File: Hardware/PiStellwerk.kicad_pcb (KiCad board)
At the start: 2 copper layers, 65 x 56 mm, 59 parts, among them J1 Conn_02x20_Odd_Even, J2 Screw_Terminal_01x02, J3 Screw_Terminal_01x02, J4 Conn_01x01, J5 Conn_01x01, J6 Conn_02x03_Odd_Even, J7 Screw_Terminal_01x02, Q1 Q_PMOS_GDS, U1 STM32G031KxT, U2 HT7533, U3 DRV8876, U4 RT8279, U5 6N136, U6 6N136, U7 RT8279, U8 DS18B20

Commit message: Change from STM32G0 to STM32F103C8T6
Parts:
- removed D2, D3: SS54, Diode_SMD:D_SMB_Handsoldering
- removed L2: 10uH, Inductor_SMD:L_7.3x7.3_H4.5
- removed R10: 100K, Resistor_SMD:R_0603_1608Metric_Pad1.05x0.95mm_HandSolder
- removed R12: R, Resistor_SMD:R_0603_1608Metric_Pad1.05x0.95mm_HandSolder
- removed R6: 10K, Resistor_SMD:R_0603_1608Metric_Pad1.05x0.95mm_HandSolder
- added C15: 35V/10nF, Capacitor_SMD:C_0603_1608Metric_Pad1.05x0.95mm_HandSolder, F.Cu at (38.7, 73.6)
- added C16: 35V/10nF, Capacitor_SMD:C_0603_1608Metric_Pad1.05x0.95mm_HandSolder, F.Cu at (48.5, 75.0)
- added C21: 6.3V/47uF, Capacitor_SMD:C_0805_2012Metric_Pad1.15x1.40mm_HandSolder, F.Cu at (20.6, 86.5)
- added C24: 35V/10uF, Capacitor_SMD:C_0805_2012Metric_Pad1.15x1.40mm_HandSolder, F.Cu at (25.2, 82.9)
- added C25: 35V/10nF, Capacitor_SMD:C_0603_1608Metric_Pad1.05x0.95mm_HandSolder, F.Cu at (50.7, 62.0)
- added C26: 6.3V/47uF, Capacitor_SMD:C_0805_2012Metric_Pad1.15x1.40mm_HandSolder, F.Cu at (30.9, 81.4)
- added C27: 35V/100nF, Capacitor_SMD:C_0603_1608Metric_Pad1.05x0.95mm_HandSolder, F.Cu at (44.2, 80.7)
- added C28: 35V/100nF, Capacitor_SMD:C_0603_1608Metric_Pad1.05x0.95mm_HandSolder, F.Cu at (25.1, 85.6)
- added C29: 35V/100nF, Capacitor_SMD:C_0603_1608Metric_Pad1.05x0.95mm_HandSolder, F.Cu at (35.5, 76.1)
- added C30: 35V/100nF, Capacitor_SMD:C_0603_1608Metric_Pad1.05x0.95mm_HandSolder, F.Cu at (25.1, 88.1)
- added C31: 35V/100nF, Capacitor_SMD:C_0603_1608Metric_Pad1.05x0.95mm_HandSolder, F.Cu at (43.4, 70.7)
- added C32: 35V/100nF, Capacitor_SMD:C_0603_1608Metric_Pad1.05x0.95mm_HandSolder, F.Cu at (35.5, 78.6)
- added C33: 35V/100nF, Capacitor_SMD:C_0603_1608Metric_Pad1.05x0.95mm_HandSolder, F.Cu at (46.7, 67.4)
- added C34: 35V/10nF, Capacitor_SMD:C_0603_1608Metric_Pad1.05x0.95mm_HandSolder, F.Cu at (29.8, 84.1)
- added C35: 35V/100nF, Capacitor_SMD:C_0603_1608Metric_Pad1.05x0.95mm_HandSolder, F.Cu at (55.4, 59.0)
- added C40: 35V/100uF, Capacitor_THT:CP_Radial_D6.3mm_P2.50mm, F.Cu at (26.0, 73.0)
- added C41: 35V/100uF, Capacitor_THT:CP_Radial_D6.3mm_P2.50mm, F.Cu at (13.1, 85.4)
- added J8: Conn_01x06, Connector_PinSocket_2.54mm:PinSocket_1x06_P2.54mm_Vertical, F.Cu at (56.4, 75.8)
- added J9: Conn_01x05, Connector_PinHeader_2.54mm:PinHeader_1x05_P2.54mm_Vertical, F.Cu at (61.0, 75.8)
- added JP1: Jumper, Connector_PinHeader_2.54mm:PinHeader_1x02_P2.54mm_Vertical, F.Cu at (20.5, 80.2)
- added JP2: Jumper, Connector_PinHeader_2.54mm:PinHeader_1x02_P2.54mm_Vertical, F.Cu at (41.4, 60.1)
- added L10: 3.3uH, Inductor_SMD:L_6.3x6.3_H3, F.Cu at (34.8, 61.7)
- added L11: 3.3uH, Inductor_SMD:L_6.3x6.3_H3, F.Cu at (5.97, 85.4)
- added L12: 3.3uH, Inductor_SMD:L_6.3x6.3_H3, F.Cu at (18.9, 73.9)
- added R14: 100K, Resistor_SMD:R_0603_1608Metric_Pad1.05x0.95mm_HandSolder, F.Cu at (44.2, 78.2)
- added R15: 13.7K, Resistor_SMD:R_0603_1608Metric_Pad1.05x0.95mm_HandSolder, F.Cu at (55.4, 67.0)
- added R16: 100K, Resistor_SMD:R_0603_1608Metric_Pad1.05x0.95mm_HandSolder, F.Cu at (34.1, 84.1)
- added R17: 13.7K, Resistor_SMD:R_0603_1608Metric_Pad1.05x0.95mm_HandSolder, F.Cu at (52.1, 72.0)
- added R19: 100K, Resistor_SMD:R_0603_1608Metric_Pad1.05x0.95mm_HandSolder, F.Cu at (47.8, 69.9)
- added R30: 22.1K, Resistor_SMD:R_0603_1608Metric_Pad1.05x0.95mm_HandSolder, F.Cu at (51.0, 67.0)
- added R40: 24R, Resistor_SMD:R_0603_1608Metric_Pad1.05x0.95mm_HandSolder, F.Cu at (39.8, 78.6)
- added R41: 24R, Resistor_SMD:R_0603_1608Metric_Pad1.05x0.95mm_HandSolder, F.Cu at (51.0, 64.5)
- added R42: 24R, Resistor_SMD:R_0603_1608Metric_Pad1.05x0.95mm_HandSolder, F.Cu at (39.8, 81.1)
- added R43: 24R, Resistor_SMD:R_0603_1608Metric_Pad1.05x0.95mm_HandSolder, F.Cu at (33.8, 86.6)
- added R50: 40K, Resistor_SMD:R_0603_1608Metric_Pad1.05x0.95mm_HandSolder, F.Cu at (47.8, 72.4)
- added R51: 40K, Resistor_SMD:R_0603_1608Metric_Pad1.05x0.95mm_HandSolder, F.Cu at (55.4, 64.5)
- added R52: 40K, Resistor_SMD:R_0603_1608Metric_Pad1.05x0.95mm_HandSolder, F.Cu at (44.2, 75.7)
- added R53: 40K, Resistor_SMD:R_0603_1608Metric_Pad1.05x0.95mm_HandSolder, F.Cu at (55.0, 62.0)
- added U9: SY8303, Package_TO_SOT_SMD:TSOT-23-8, F.Cu at (25.8, 79.2)
- C11: value 35V/10uF -> 35V/10nF; footprint Capacitor_SMD:C_0805_2012Metric_Pad1.15x1.40mm_HandSolder -> Capacitor_SMD:C_0603_1608Metric_Pad1.05x0.95mm_HandSolder
- C13, C14: value 35V/10nF -> 35V/10uF; footprint Capacitor_SMD:C_0603_1608Metric_Pad1.05x0.95mm_HandSolder -> Capacitor_SMD:C_0805_2012Metric_Pad1.15x1.40mm_HandSolder
- C18: value 35V/470uF -> 35V/100nF; footprint Capacitor_THT:CP_Radial_D8.0mm_P3.50mm -> Capacitor_SMD:C_0603_1608Metric_Pad1.05x0.95mm_HandSolder
- C19: value 35V/10uF -> 35V/100nF; footprint Capacitor_SMD:C_0805_2012Metric_Pad1.15x1.40mm_HandSolder -> Capacitor_SMD:C_0603_1608Metric_Pad1.05x0.95mm_HandSolder
- C2: value 6.3V/470uF -> 35V/10uF; footprint Capacitor_THT:CP_Radial_D6.3mm_P2.50mm -> Capacitor_SMD:C_0805_2012Metric_Pad1.15x1.40mm_HandSolder
- D1: value 10V -> 12V; footprint Diode_SMD:D_SMA -> Diode_SMD:D_MiniMELF
- J6: value Conn_02x03_Odd_Even -> Conn_01x01; footprint Connector_PinHeader_2.54mm:PinHeader_2x03_P2.54mm_Vertical -> Connector_PinHeader_2.54mm:PinHeader_1x01_P2.54mm_Vertical
- J7: value Screw_Terminal_01x02 -> Conn_01x04; footprint TerminalBlock_Phoenix:TerminalBlock_Phoenix_MKDS-1,5-2-5.08_1x02_P5.08mm_Horizontal -> Connector_PinSocket_2.54mm:PinSocket_1x04_P2.54mm_Vertical
- Q1: footprint Package_TO_SOT_SMD:TO-252-3_TabPin2 -> Package_TO_SOT_SMD:SOT-23
- R11: value 31K6 -> 10K
- R5: value 1K -> 10K
- R9: value 7K32 -> 3.4K
- U1: value STM32G031KxT -> STM32F103C8Tx; footprint Package_QFP:LQFP-32_7x7mm_P0.8mm -> Package_QFP:LQFP-48_7x7mm_P0.5mm
- U4, U7: value RT8279 -> SY8303; footprint Package_SO:HSOP-8-1EP_3.9x4.9mm_P1.27mm_EP2.41x3.1mm -> Package_TO_SOT_SMD:TSOT-23-8
- U5: value 6N136 -> ADUM4160; footprint Package_DIP:SMDIP-8_W7.62mm -> Package_SO:SOIC-16W_7.5x10.3mm_P1.27mm
- U6: value 6N136 -> ISO3088DW; footprint Package_DIP:SMDIP-8_W7.62mm -> Package_SO:SOIC-16W_7.5x10.3mm_P1.27mm
- U8: value DS18B20 -> SY8303; footprint Package_TO_SOT_THT:TO-92_Inline_Horizontal1 -> Package_TO_SOT_SMD:TSOT-23-8
- moved J6 69.5 mm to (65.6, 75.8)
- moved R11 68.6 mm to (38.5, 83.7)
- moved C12 57.8 mm to (38.9, 70.9), turned to 0 degrees
- moved R7 56.6 mm to (43.4, 73.2), turned to 0 degrees
- moved U7 56.1 mm to (33.8, 72.3), turned to 0 degrees
- moved C17 55.5 mm to (46.1, 59.2), turned to 0 degrees
- moved C2 53.8 mm to (50.9, 59.2), turned to 0 degrees
- moved U6 48.8 mm to (8.15, 63.7), turned to 0 degrees
- moved U5 48.4 mm to (8.15, 75.5), turned to 0 degrees
- moved C14 48.0 mm to (46.1, 62.2), turned to 0 degrees
- moved C11 41.8 mm to (38.5, 86.2), turned to 0 degrees
- moved U8 41.0 mm to (41.8, 67.2)
- moved U1 40.7 mm to (24.9, 63.4), turned to 0 degrees
- moved C19 38.2 mm to (52.1, 69.5), turned to 0 degrees
- moved R8 32.4 mm to (29.5, 86.6)
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- renumbered L1 to L0
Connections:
- C11 pad 1: GND -> Net-(C11-Pad1)
- C11 pad 2: VIN -> Net-(C11-Pad2)
- C13 pad 1: Net-(C13-Pad1) -> 18V
- C13 pad 2: Net-(C13-Pad2) -> GND
- C14 pad 1: Net-(C14-Pad1) -> GND
- C14 pad 2: Net-(C14-Pad2) -> VIN
- C18 pad 1: VIN -> /USB+
- C18 pad 2: GND -> /USB_GND
- C19 pad 1: 18V -> /USB_VDD
- C19 pad 2: GND -> /USB_GND
- C2 pad 1: /3V3_UNFILTERED -> GND
- C2 pad 2: GND -> VIN
- C20 pad 1: 18V -> Net-(C20-Pad1)
- C20 pad 2: GND -> Net-(C20-Pad2)
- C4 pad 1: GND -> 3V3
- C4 pad 2: +3V3 -> GND
- C7 pad 1: +3V3 -> 3VA3
- FB1 pad 1: +3V3 -> 3VA3
- J6 pad 1: NRST -> Net-(C30-Pad1)
- J7 pad 1: Net-(J7-Pad1) -> /USB+
- L0 pad 2: Net-(C13-Pad2) -> Net-(C11-Pad2)
- Q1 pad 2: Net-(J3-Pad2) -> VIN
- Q1 pad 3: VIN -> Net-(J3-Pad2)
- R11 pad 1: Net-(R10-Pad2) -> EN_SEC_5V
- R5 pad 1: Net-(R5-Pad1) -> ENABLE_18V
- R5 pad 2: Net-(J7-Pad2) -> GND
- U1 pad 1: (no net) -> 3V3
- U1 pad 11: SPI_SS -> (no net)
- U1 pad 13: SPI_MISO -> (no net)
- U1 pad 14: (no net) -> SPI_SS
- U1 pad 15: (no net) -> SPI_SCLK
- U1 pad 16: TRACK_CURRENT -> SPI_MISO
- U1 pad 17: (no net) -> SPI_MOSI
- U1 pad 19: nFault -> TRACK_CURRENT
- U1 pad 20: (no net) -> nSleep
- U1 pad 21: nSleep -> nFault
- U1 pad 22: IN2 -> IN1
- U1 pad 23: IN1 -> GND
- U1 pad 24: SWDIO -> 3V3
- U1 pad 25: SWCLK -> IN2
- U1 pad 27: /SENSE_TEMP -> (no net)
- U1 pad 28: ENABLE_18V -> (no net)
- U1 pad 29: TRACK_IN_1 -> USB_PIN
- U1 pad 30: TRACK_IN_2 -> UART_TX
- U1 pad 31: (no net) -> UART_RX
- U1 pad 32: ENABLE_5V -> USB_D-
- U1 pad 4: +3V3 -> (no net)
- U1 pad 5: GND -> (no net)
- U1 pad 6: NRST -> (no net)
- U1 pad 7: (no net) -> Net-(C30-Pad1)
- U1 pad 8: SPI_SCLK -> GND
- U1 pad 9: SPI_MOSI -> 3VA3
- U4 pad 1: Net-(C13-Pad1) -> Net-(R8-Pad2)
- U4 pad 2: (no net) -> Net-(R53-Pad2)
- U4 pad 3: (no net) -> GND
- U4 pad 4: Net-(R8-Pad2) -> GND
- U4 pad 5: ENABLE_18V -> VIN
- U4 pad 6: GND -> Net-(C11-Pad2)
- U4 pad 7: VIN -> Net-(C11-Pad1)
- U4 pad 8: Net-(C13-Pad2) -> ENABLE_18V
- U5 pad 1: (no net) -> /USB+
- U5 pad 2: Net-(J7-Pad1) -> /USB_GND
- U5 pad 3: Net-(R5-Pad1) -> /USB_VDD
- U5 pad 4: (no net) -> /USB_VDD
- U5 pad 5: GND -> /USB_VDD
- U5 pad 6: TRACK_IN_1 -> Net-(R43-Pad1)
- U5 pad 7: (no net) -> Net-(R42-Pad2)
- U5 pad 8: +3V3 -> /USB_GND
- U6 pad 1: (no net) -> Net-(C20-Pad2)
- U6 pad 2: Net-(R5-Pad1) -> Net-(C20-Pad1)
- U6 pad 3: Net-(J7-Pad1) -> Net-(J8-Pad3)
- U6 pad 4: (no net) -> Net-(J8-Pad2)
- U6 pad 5: GND -> Net-(J8-Pad5)
- U6 pad 6: TRACK_IN_2 -> Net-(J8-Pad4)
- U6 pad 7: (no net) -> Net-(C20-Pad1)
- U6 pad 8: +3V3 -> Net-(C20-Pad1)
- U7 pad 1: Net-(C14-Pad1) -> Net-(R14-Pad2)
- U7 pad 2: (no net) -> Net-(R50-Pad2)
- U7 pad 3: (no net) -> GND
- U7 pad 4: Net-(R10-Pad2) -> GND
- U7 pad 5: ENABLE_5V -> VIN
- U7 pad 6: GND -> Net-(C15-Pad2)
- U7 pad 7: VIN -> Net-(C15-Pad1)
- U7 pad 8: Net-(C14-Pad2) -> ENABLE_5V
- U8 pad 1: GND -> Net-(R19-Pad2)
- U8 pad 2: /SENSE_TEMP -> Net-(R51-Pad2)
- U8 pad 3: +3V3 -> GND
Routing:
- net GND: track 156.8 -> 96.5 mm, vias 119 -> 41
- net Net-(C13-Pad2): track 15.7 -> 0.00 mm
- net Net-(C11-Pad2): track 0.00 -> 15.7 mm

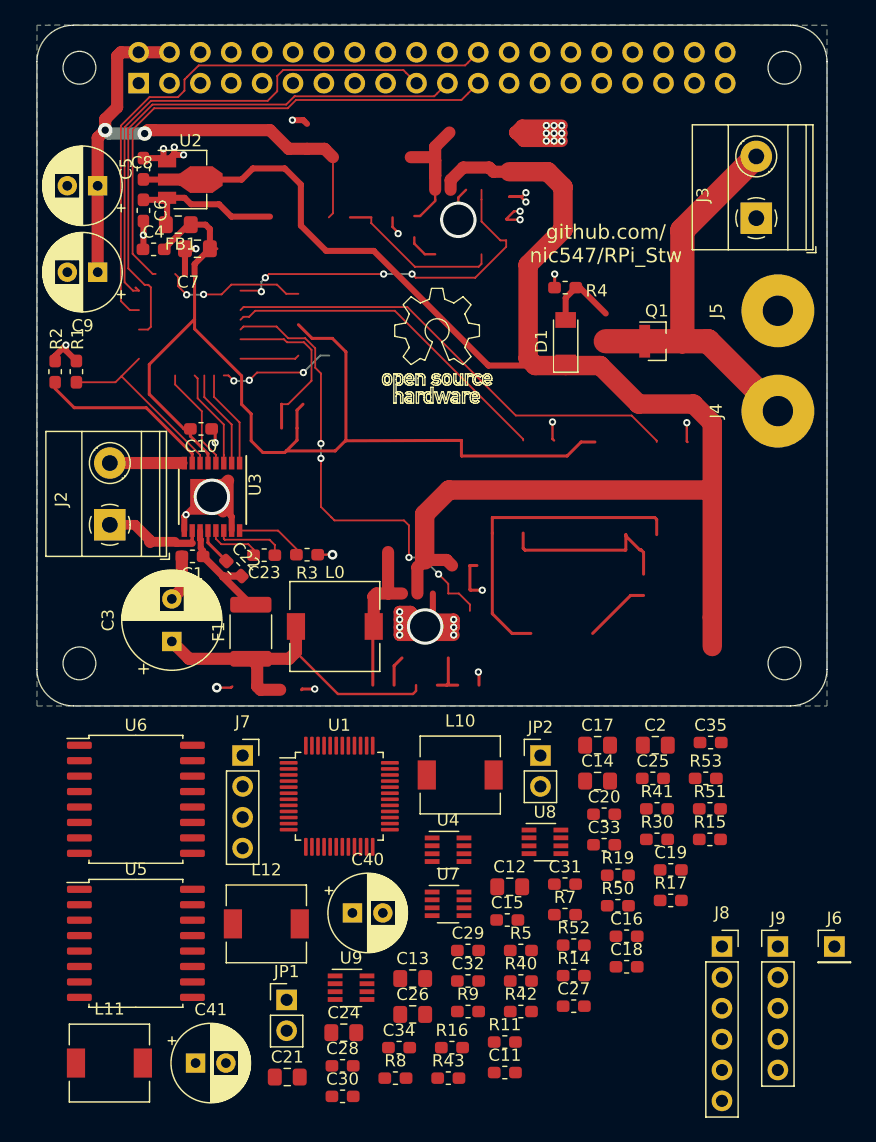
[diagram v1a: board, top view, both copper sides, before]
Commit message: Add CubeMX project and reworked pcb
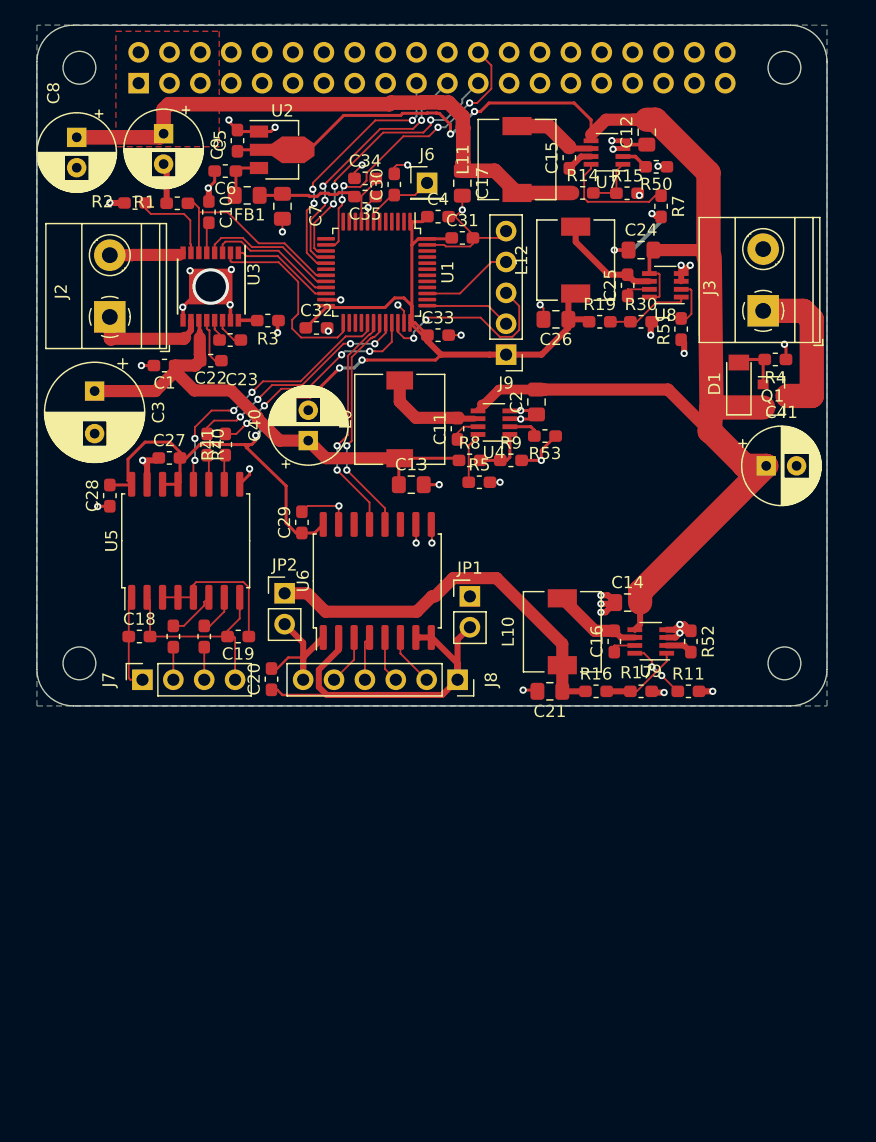
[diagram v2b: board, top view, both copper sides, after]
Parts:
- removed F1: Polyfuse, Fuse:Fuse_1812_4532Metric_Pad1.30x3.40mm_HandSolder
- removed J4, J5: Conn_01x01, Connector_Wire:SolderWirePad_1x01_Drill2.5mm
- C3: value 35V/470uF -> 35V/220uF
- moved L11 81.5 mm to (39.5, 11.1), turned to 90 degrees
- moved C30 75.1 mm to (29.4, 13.1), turned to 90 degrees
- moved C34 71.6 mm to (27.0, 12.6)
- moved J6 71.2 mm to (32.1, 13.0)
- moved C24 68.9 mm to (49.7, 18.5)
- moved C41 68.0 mm to (60.0, 36.2)
- moved R14 64.4 mm to (44.9, 13.8)
- moved U7 63.2 mm to (46.9, 10.5), turned to 180 degrees
- moved C12 63.1 mm to (50.2, 8.80), turned to 90 degrees
- moved C15 62.9 mm to (43.8, 10.9), turned to 90 degrees
- moved R50 60.9 mm to (51.0, 11.7), turned to 180 degrees
- moved L12 60.2 mm to (44.3, 19.3), turned to 90 degrees
- moved R7 58.8 mm to (51.4, 14.9), turned to 270 degrees
- moved C26 58.4 mm to (42.7, 24.2), turned to 180 degrees
- moved C27 56.0 mm to (10.9, 35.6)
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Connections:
- C1 pad 1: Net-(C1-Pad1) -> 18V
- C22 pad 2: Net-(C1-Pad1) -> 18V
- J3 pad 1: GND -> Net-(J3-Pad1)
- J3 pad 2: Net-(J3-Pad2) -> GND
- J9 pad 2: (no net) -> SWCLK
- J9 pad 3: (no net) -> SWDIO
- Q1 pad 3: Net-(J3-Pad2) -> Net-(J3-Pad1)
- R42 pad 1: Net-(J7-Pad2) -> Net-(J7-Pad3)
- R43 pad 2: Net-(J7-Pad3) -> Net-(J7-Pad2)
- U1 pad 20: nSleep -> nFault
- U1 pad 21: nFault -> nSleep
- U1 pad 34: (no net) -> SWDIO
- U1 pad 37: (no net) -> SWCLK
- U3 pad 11: Net-(C1-Pad1) -> 18V
- U6 pad 3: Net-(J8-Pad3) -> Net-(J8-Pad5)
- U6 pad 4: Net-(J8-Pad2) -> Net-(J8-Pad4)
- U6 pad 5: Net-(J8-Pad5) -> Net-(J8-Pad3)
- U6 pad 6: Net-(J8-Pad4) -> Net-(J8-Pad2)
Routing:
- net 3V3: track 0.00 -> 104.5 mm, vias 0 -> 4
- net +3V3: track 88.3 -> 2.55 mm
- net TRACK_IN_2: track 39.0 -> 0.00 mm
- net Net-(J3-Pad2): track 34.3 -> 0.00 mm
- net ENABLE_18V: track 38.4 -> 4.37 mm, vias 4 -> 0
- net Net-(C21-Pad1): track 0.00 -> 32.7 mm
- net Net-(C20-Pad1): track 0.00 -> 32.1 mm
- net TRACK_IN_1: track 28.1 -> 0.00 mm
- net Net-(J7-Pad1): track 26.6 -> 0.00 mm
- net SPI_MISO: track 46.8 -> 21.6 mm, vias 0 -> 3
- net SPI_SS: track 48.7 -> 25.2 mm, vias 0 -> 4
- net USB_PIN: track 0.00 -> 22.9 mm, vias 0 -> 4
- net SPI_MOSI: track 41.8 -> 21.5 mm, vias 0 -> 3
- net ENABLE_5V: track 30.0 -> 9.68 mm, vias 4 -> 0
- net UART_RX: track 0.00 -> 20.1 mm, vias 0 -> 2
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- added copper zone on F.Cu, net 5V
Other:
- board text removed: "github.com/ nic547/RPi_Stw"

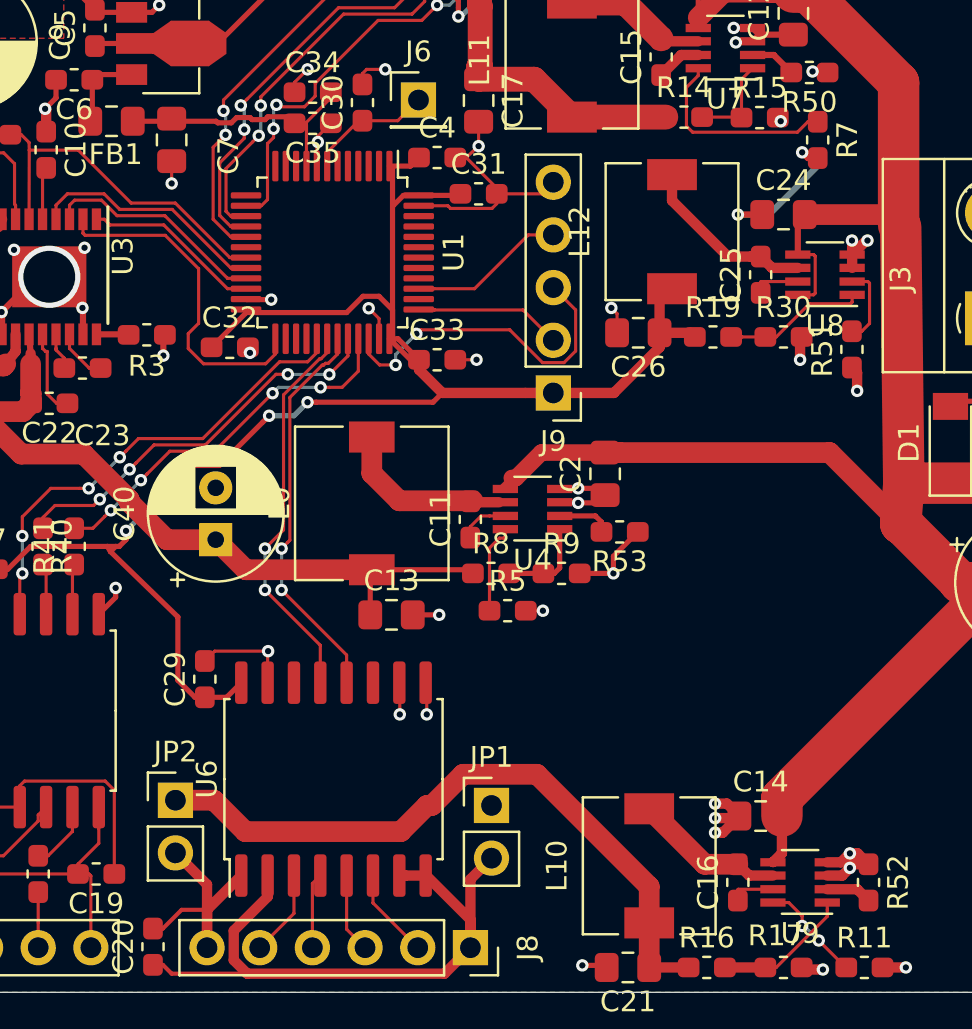
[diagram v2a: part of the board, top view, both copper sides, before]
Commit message: connect enable pins of bucks to mcu
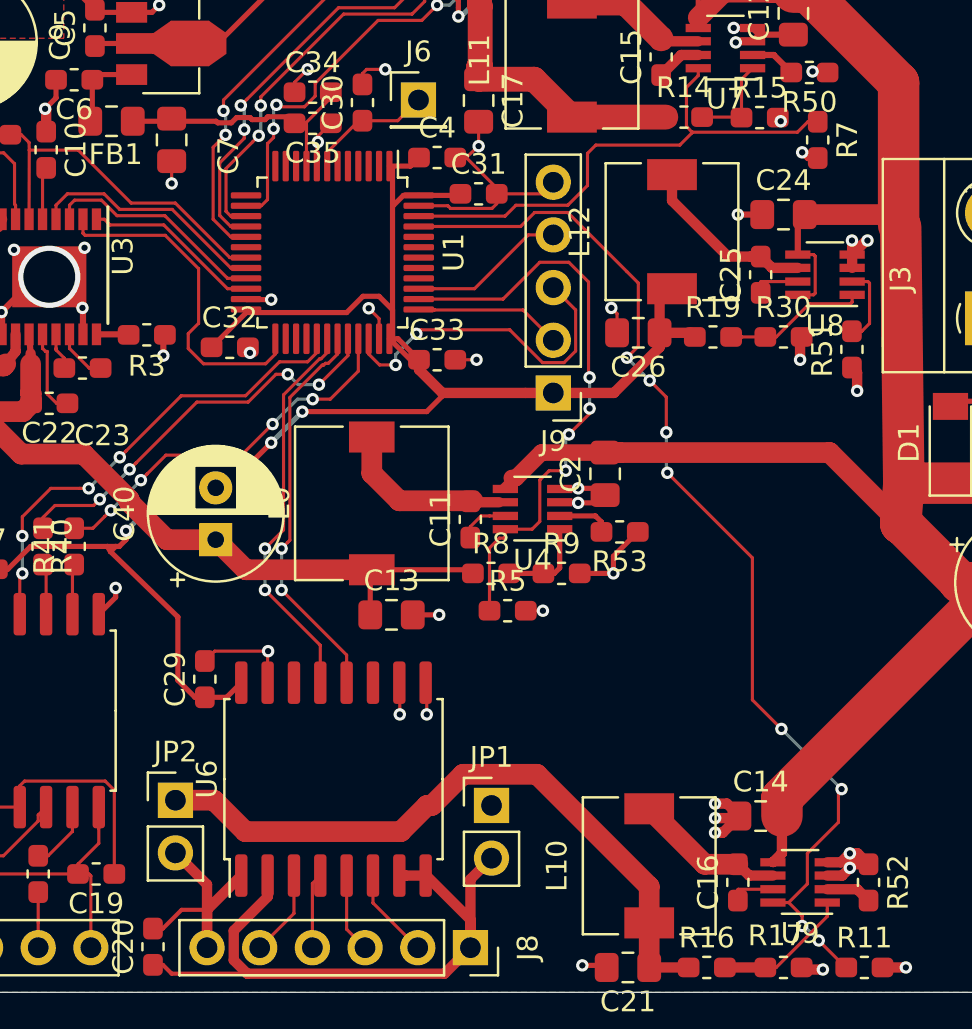
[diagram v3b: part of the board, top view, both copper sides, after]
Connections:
- U1 pad 38: (no net) -> ENABLE_18V
- U1 pad 45: (no net) -> EN_SEC_5V
- U1 pad 46: (no net) -> ENABLE_5V
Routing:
- net EN_SEC_5V: track 5.11 -> 52.8 mm, vias 2 -> 8
- net ENABLE_18V: track 4.37 -> 28.5 mm, vias 0 -> 4
- net ENABLE_5V: track 9.68 -> 25.5 mm
- net GND: track 104.8 -> 99.8 mm
